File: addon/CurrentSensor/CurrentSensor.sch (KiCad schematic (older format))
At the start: 3 parts, among them J102 Conn_01x08_Male, J103 Conn_01x08_Male

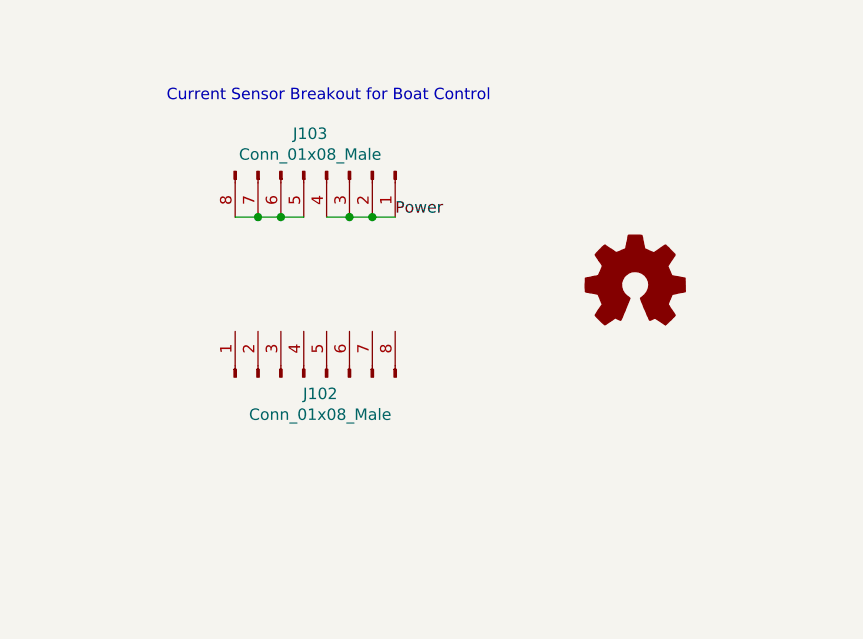
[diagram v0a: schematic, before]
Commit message: Add current sensor
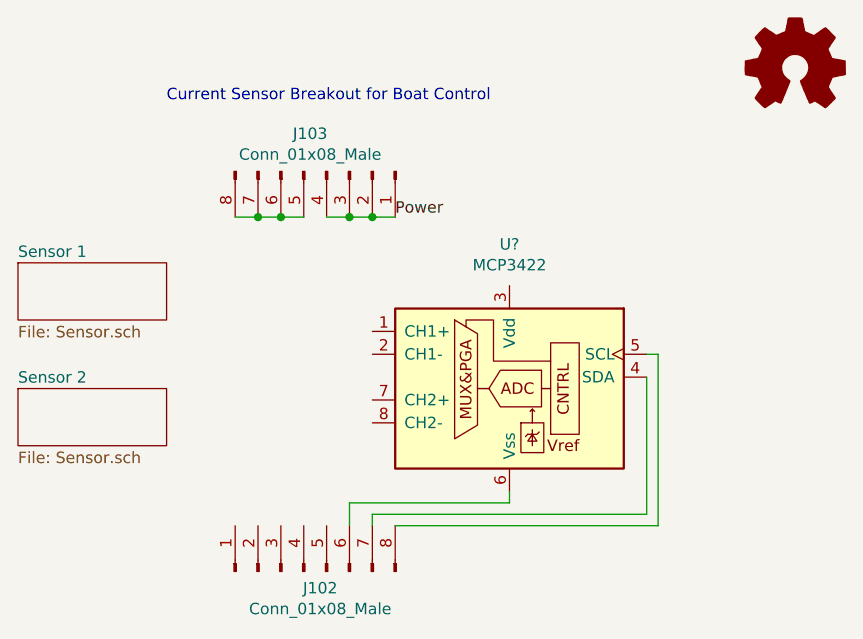
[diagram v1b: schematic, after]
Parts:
- added U?: MCP3422, symbol Analog_ADC:MCP3422
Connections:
- net at J102.6 (Pin_6): now also U?.6 (Vss)
- net at J102.7 (Pin_7): now also U?.4 (SDA)
- net at J102.8 (Pin_8): now also U?.5 (SCL)
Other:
- moved on the sheet: J102
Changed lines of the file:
@@
 $Descr A4 11693 8268
 encoding utf-8
-Sheet 1 1
+Sheet 1 3
 Title "Current Sensor Breakout"
 Date "2021-01-05"
@@
 L Graphic:Logo_Open_Hardware_Small LOGO101
 U 1 1 5FF5287F
-P 6900 3900
-F 0 "LOGO101" H 6900 4175 50  0001 C CNN
-F 1 "Logo_Open_Hardware_Small" H 6900 3675 50  0001 C CNN
-F 2 "CurrentShunt:OSHW-Logo2_7.3x6mm_SilkScreen" H 6900 3900 50  0001 C CNN
-F 3 "~" H 6900 3900 50  0001 C CNN
-	1    6900 3900
+P 7600 2950
+F 0 "LOGO101" H 7600 3225 50  0001 C CNN
+F 1 "Logo_Open_Hardware_Small" H 7600 2725 50  0001 C CNN
+F 2 "CurrentShunt:OSHW-Logo2_7.3x6mm_SilkScreen" H 7600 2950 50  0001 C CNN
+F 3 "~" H 7600 2950 50  0001 C CNN
+	1    7600 2950
 	1    0    0    -1
 $EndComp
@@
 L Connector:Conn_01x08_Male J102
 U 1 1 5FF48021
-P 5450 4300
-F 0 "J102" V 5377 4228 50  0000 C CNN
-F 1 "Conn_01x08_Male" V 5286 4228 50  0000 C CNN
-F 2 "Connector_PinHeader_2.54mm:PinHeader_1x08_P2.54mm_Vertical" H 5450 4300 50  0001 C CNN
-F 3 "~" H 5450 4300 50  0001 C CNN
-	1    5450 4300
+P 5450 5150
+F 0 "J102" V 5377 5078 50  0000 C CNN
+F 1 "Conn_01x08_Male" V 5286 5078 50  0000 C CNN
+F 2 "Connector_PinHeader_2.54mm:PinHeader_1x08_P2.54mm_Vertical" H 5450 5150 50  0001 C CNN
+F 3 "~" H 5450 5150 50  0001 C CNN
+	1    5450 5150
 	0    -1   -1   0
 $EndComp
@@
 	5850 3600 5750 3600
 Connection ~ 5750 3600
-Wire Wire Line
-	5750 3600 5650 3600
 Connection ~ 5650 3600
 Wire Wire Line
@@
 Wire Wire Line
 	5450 3600 5350 3600
-Wire Wire Line
-	5250 3600 5350 3600
 Connection ~ 5350 3600
 Wire Wire Line
 	5150 3600 5250 3600
 Connection ~ 5250 3600
+$Comp
+L Analog_ADC:MCP3422 U?
+U 1 1 5FF42BE9
+P 6350 4300
+F 0 "U?" H 6350 4881 50  0000 C CNN
+F 1 "MCP3422" H 6350 4790 50  0000 C CNN
+F 2 "" H 7250 4000 50  0001 C CNN
+F 3 "http://ww1.microchip.com/downloads/en/DeviceDoc/22088c.pdf" H 7250 4000 50  0001 C CNN
+	1    6350 4300
+	1    0    0    -1
+$EndComp
+Wire Wire Line
+	5650 3600 5750 3600
+Wire Wire Line
+	5250 3600 5350 3600
+$Sheet
+S 4200 3800 650  250
+U 5FF51AE2
+F0 "Sensor 1" 50
+F1 "Sensor.sch" 50
+$EndSheet
+$Sheet
+S 4200 4350 650  250
+U 5FF53ADE
+F0 "Sensor 2" 50
+F1 "Sensor.sch" 50
+$EndSheet
+Wire Wire Line
+	6350 4800 6350 4850
+Wire Wire Line
+	6350 4850 5650 4850
+Wire Wire Line
+	5650 4850 5650 4950
+Wire Wire Line
+	6950 4300 6950 4900
+Wire Wire Line
+	6950 4900 5750 4900
+Wire Wire Line
+	5750 4900 5750 4950
+Wire Wire Line
+	6950 4200 7000 4200
+Wire Wire Line
+	7000 4200 7000 4950
+Wire Wire Line
+	7000 4950 5850 4950
 $EndSCHEMATC

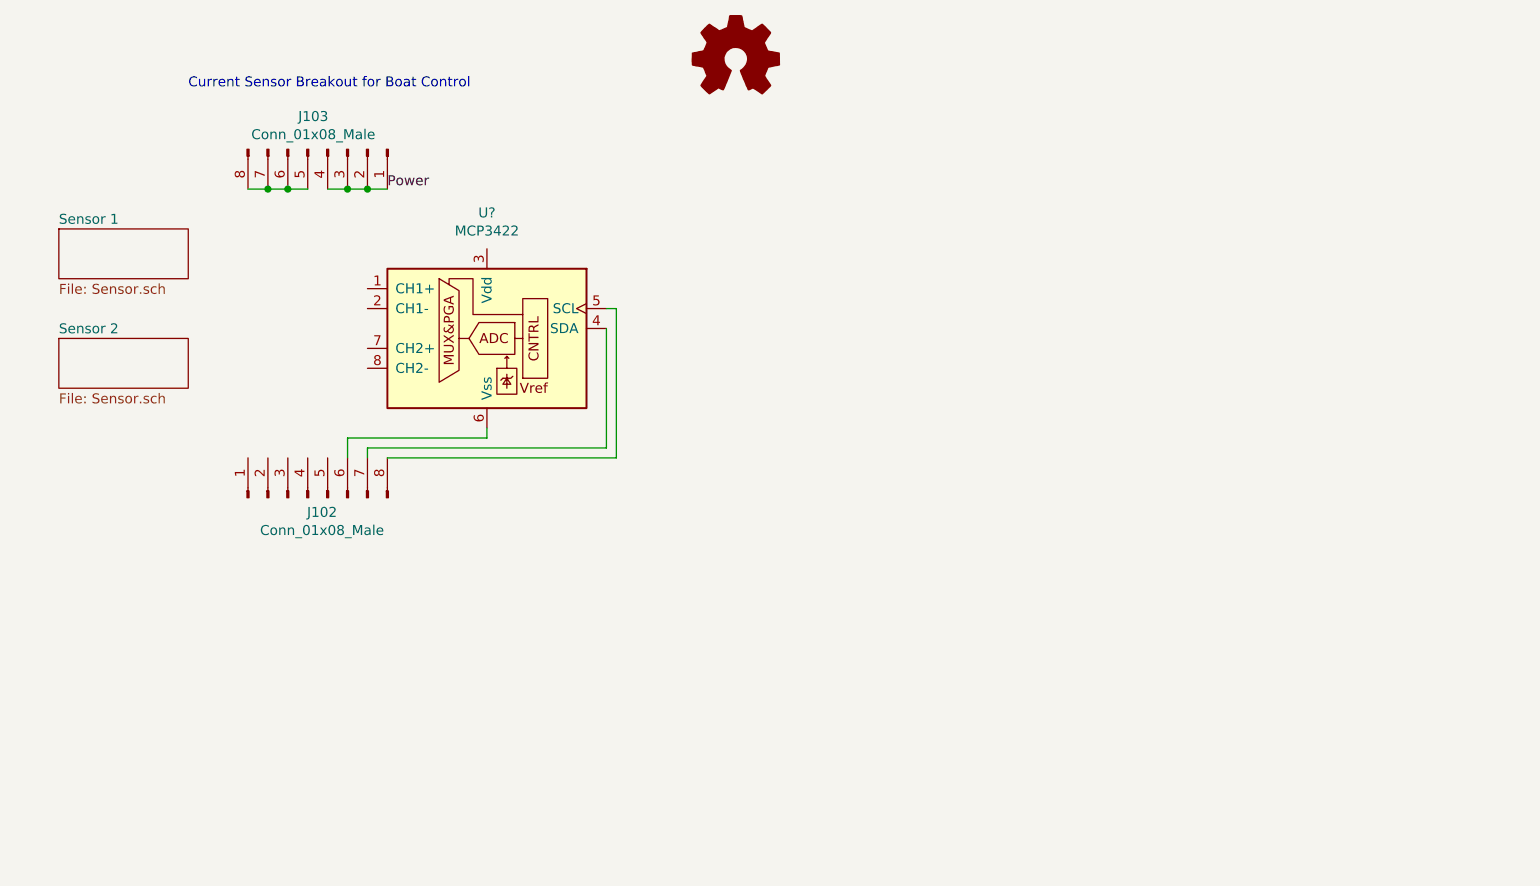
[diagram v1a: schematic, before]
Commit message: Fix power interconnects
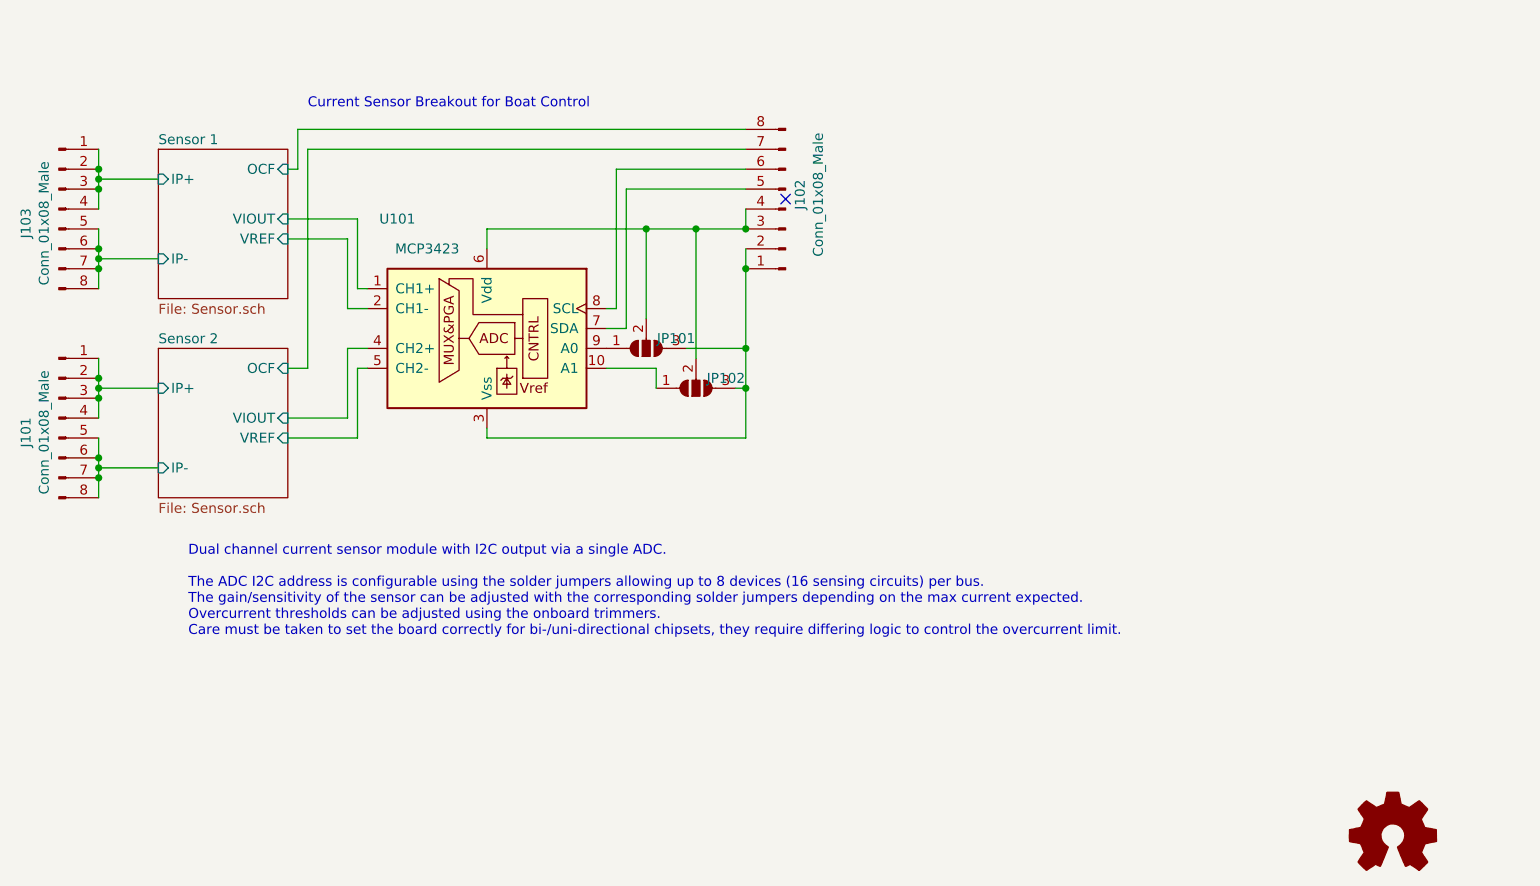
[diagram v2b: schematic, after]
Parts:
- removed U?: MCP3422, symbol Analog_ADC:MCP3422
- added J101: Conn_01x08_Male, Connector_PinHeader_2.54mm:PinHeader_1x08_P2.54mm_Vertical, symbol Connector:Conn_01x08_Male
- added JP101, JP102: SolderJumper_3_Open, Jumper:SolderJumper-3_P1.3mm_Open_RoundedPad1.0x1.5mm, symbol Jumper:SolderJumper_3_Open
- added U101: MCP3423, Package_SO:MSOP-10_3x3mm_P0.5mm, symbol Analog_ADC:MCP3423
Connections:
- net Sensor 2/OCF: now reaches J102.7 (Pin_7)
- net Sensor 1/OCF: now reaches J102.8 (Pin_8)
- net at J102.6 (Pin_6): now also U101.8 (SCL)
- net Sensor 1/IP-: now reaches J103.5 (Pin_5), J103.6 (Pin_6), J103.7 (Pin_7), J103.8 (Pin_8)
- net at J102.1 (Pin_1): now also J102.2 (Pin_2), JP101.3 (B), JP102.3 (B), U101.3 (Vss)
- net at J102.3 (Pin_3): now also J102.4 (Pin_4), JP101.2 (C), JP102.2 (C), U101.6 (Vdd)
- net at J102.5 (Pin_5): now also U101.7 (SDA)
- net Power renamed Sensor 1/IP+
- new net: JP102.1 (A), U101.10 (A1)
- new net: JP101.1 (A), U101.9 (A0)
- new net Sensor 1/VIOUT: U101.1 (CH1+)
- new net Sensor 1/VREF: U101.2 (CH1-)
- new net Sensor 2/IP+: J101.1 (Pin_1), J101.2 (Pin_2), J101.3 (Pin_3), J101.4 (Pin_4)
- new net Sensor 2/IP-: J101.5 (Pin_5), J101.6 (Pin_6), J101.7 (Pin_7), J101.8 (Pin_8)
- new net Sensor 2/VIOUT: U101.4 (CH2+)
- new net Sensor 2/VREF: U101.5 (CH2-)
- no-connect marks 0 -> 1
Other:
- note added: "Dual channel current sensor module with I2C output via a single ADC. \n\nThe ADC I2C address is configurable using the solder jumpers allowing up to 8 devices (16 sensing circuits) per bus.\nThe gain/sensitivity of the sensor can be adjusted with the corresponding solder jumpers depending on the max current expected.\nOvercurrent thresholds can be adjusted using the onboard trimmers.\nCare must b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"
- moved on the sheet: J102, J103
